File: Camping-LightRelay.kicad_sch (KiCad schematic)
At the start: 61 parts, among them CN1 U262-061N-4BVC11, CN2 907-152A1022D10200, CN3 907-152A1022D10200, J1 Conn_01x04_Pin, J2 Conn_01x04_Socket, Q1 FDV301N, Q2 BC817, Q3 IRF7404, U1 USBLC6-2SC6, U2 CD4011UBM, U3 SI1865DDL, U4 ME2108A50M, U5 TLC555DTR

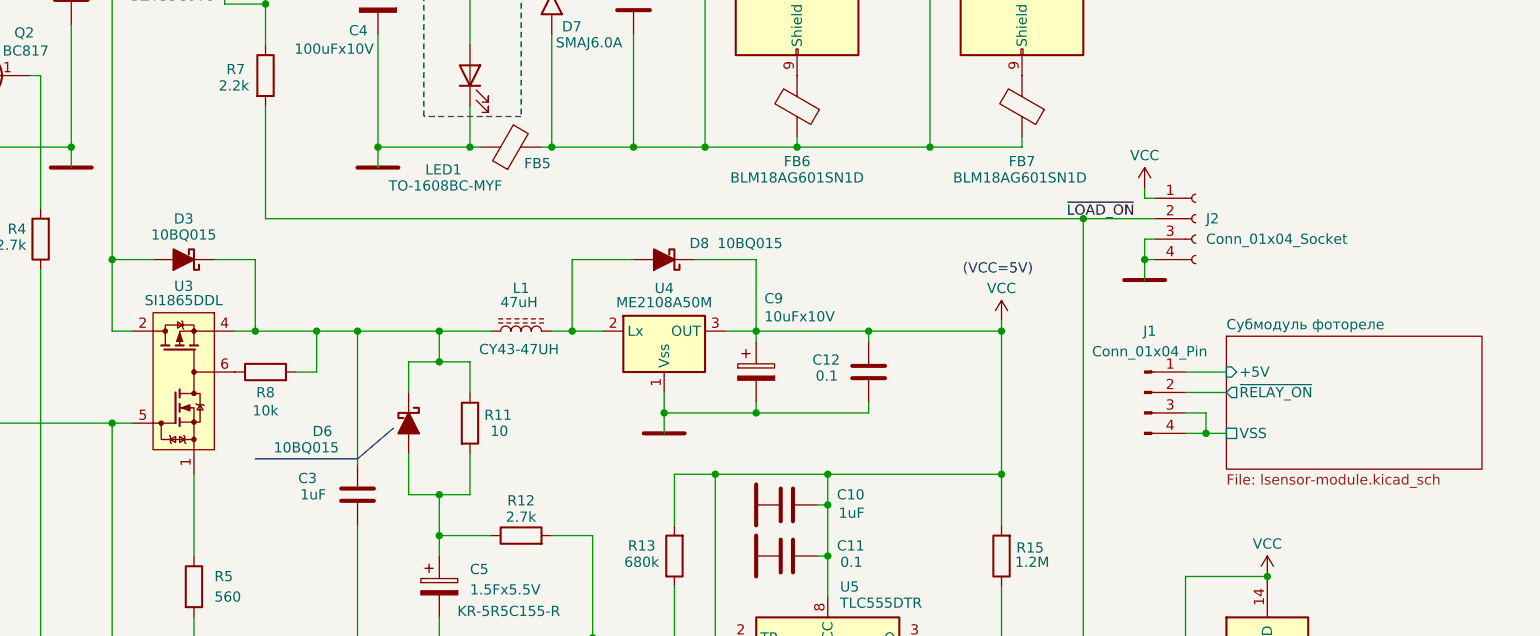
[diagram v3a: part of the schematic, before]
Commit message: Назначение посадочных мест схемы
Дорисовка недостающий э/компонентов и важных 3D-моделей
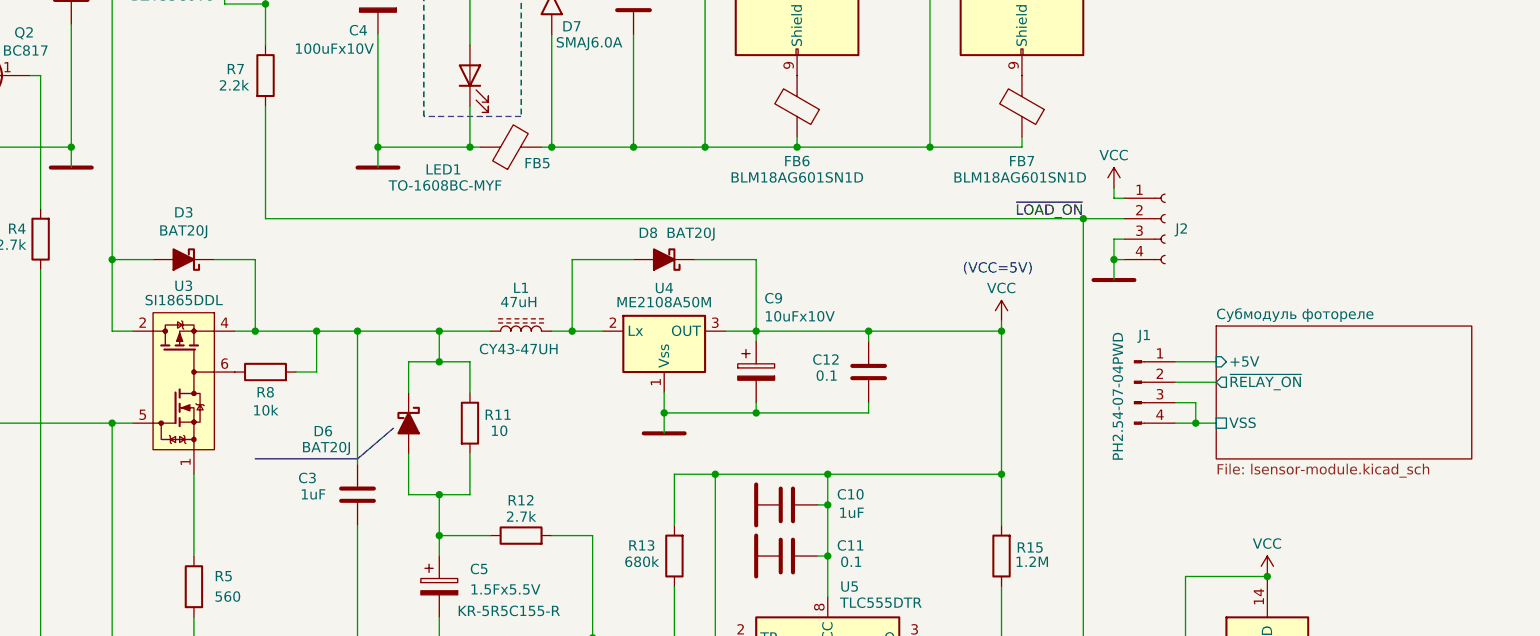
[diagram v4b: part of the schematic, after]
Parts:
- removed D3, D6, D8: 10BQ015, Diode_SMD_AKL:D_SMB, symbol PCM_Diode_Schottky_AKL:VS-10BQ015
- added D3, D6, D8: BAT20J, Diode_SMD:D_SOD-323_HandSoldering, symbol PCM_Diode_Schottky_AKL:BAT20J
- C10: footprint (none) -> Capacitor_SMD:C_0805_2012Metric
- C11, C12, C15, C6, C8: footprint (none) -> Capacitor_SMD:C_0603_1608Metric
- C5: footprint (none) -> lib:Eaton_KR-5R5C155
- J1: value Conn_01x04_Pin -> PH2.54-07-04PWD; footprint (none) -> Connector_PinHeader_2.54mm:PinHeader_1x04_P2.54mm_Horizontal
- J2: value Conn_01x04_Socket -> ~; footprint (none) -> lib:PinSolder_1x04_P2.54mm
- Q1, Q2: footprint Package_TO_SOT_SMD_AKL:SOT-23 -> PCM_Package_TO_SOT_SMD_AKL:SOT-23_BigPads
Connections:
- net VCC: now also D8.1 (K)
- net at C2.1, D4.1 (K), D5.1 (A1)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: now also D3.2 (A)
- net at C3.1, L1.1, R11.1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: now also D3.1 (K), D6.1 (K)
- net at C5.1, R11.2, R12.1: now also D6.2 (A)
- net at L1.2, U4.2 (Lx): now also D8.2 (A)
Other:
- moved on the sheet: J1, J2

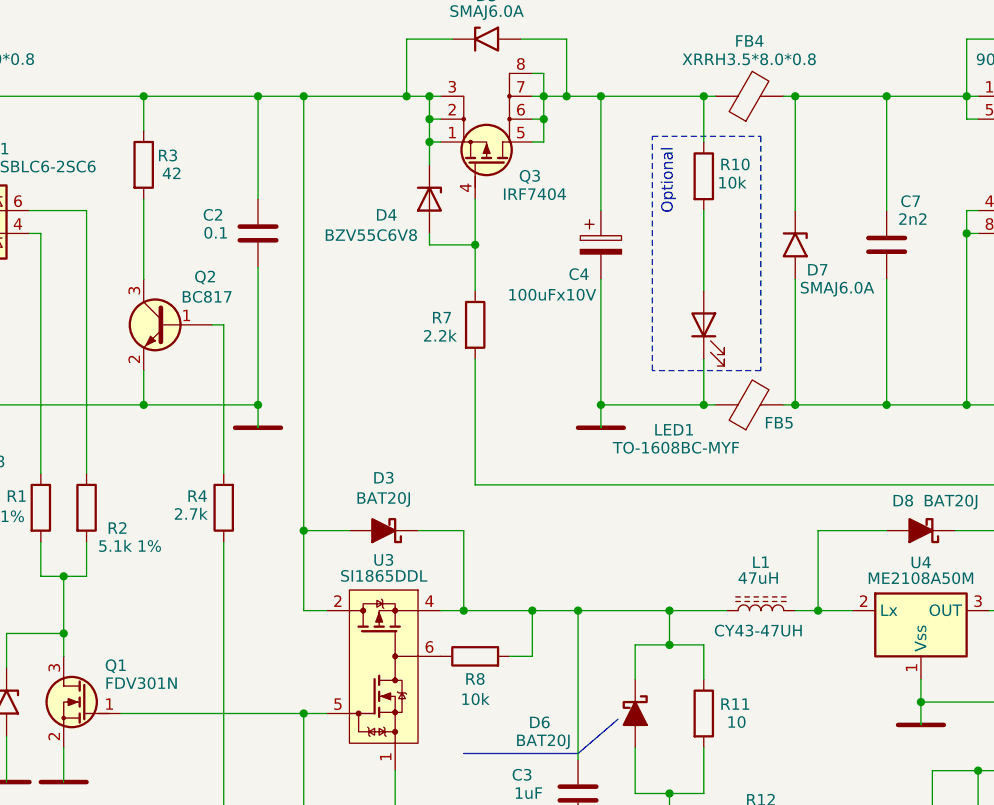
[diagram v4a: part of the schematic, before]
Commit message: Переход на 2-х стороннюю ПП
Топология ПП выбрана двусторонняя в виду миниатюрности устройства. Изменение посадочных мест под новую топологию.
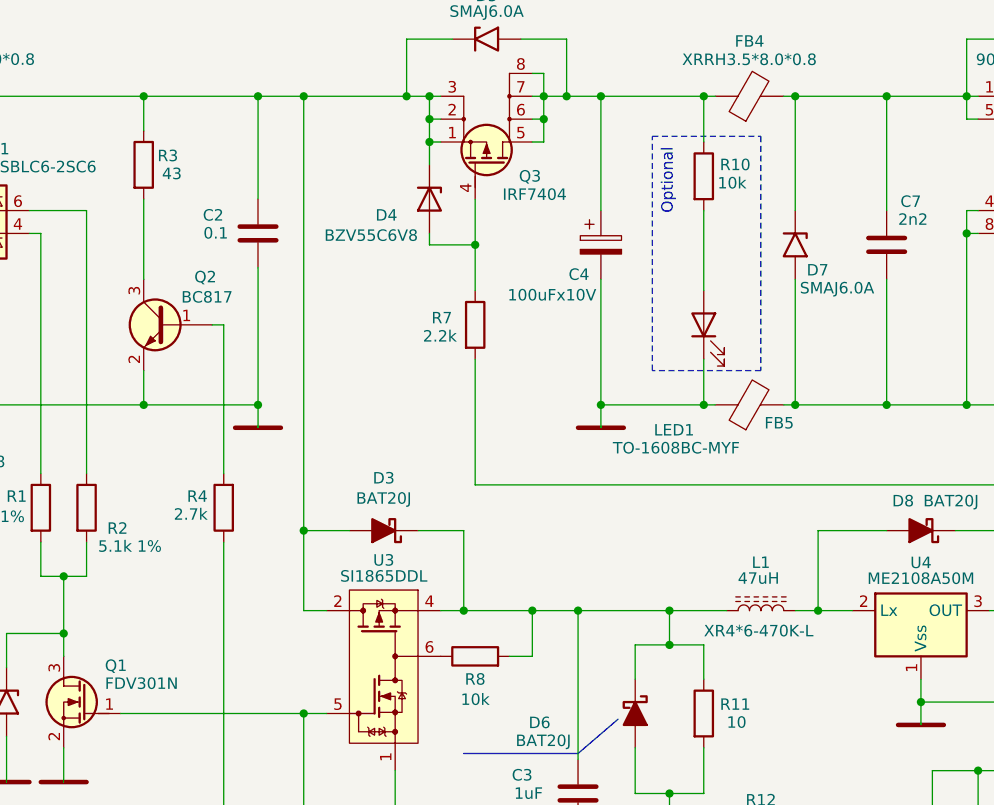
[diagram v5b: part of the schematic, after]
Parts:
- FB2, FB4: footprint PCM_Ferrite_THT_AKL:Ferrite_L8.0mm_D3.5mm_P12.70mm -> PCM_Ferrite_THT_AKL:Ferrite_L8.0mm_D3.5mm_P3.81mm_Vertical
- L1: footprint Inductor_SMD:L_Taiyo-Yuden_NR-50xx -> Inductor_THT:L_Radial_D6.0mm_P4.00mm; Part Number CY43-47UH -> XR4*6-470K-L
- Q1, Q2: footprint PCM_Package_TO_SOT_SMD_AKL:SOT-23_BigPads -> Package_TO_SOT_SMD:SOT-23
- R3: value 42 -> 43; footprint PCM_Resistor_SMD_AKL:R_0805_2012Metric_Pad1.15x1.40mm -> Resistor_THT:R_Axial_DIN0309_L9.0mm_D3.2mm_P2.54mm_Vertical
- U4: now in the parts list
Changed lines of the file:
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@@
 			)
 		)
-		(property "Footprint" "PCM_Ferrite_THT_AKL:Ferrite_L8.0mm_D3.5mm_P12.70mm"
+		(property "Footprint" "PCM_Ferrite_THT_AKL:Ferrite_L8.0mm_D3.5mm_P3.81mm_Vertical"
 			(at 69.85 30.988 90)
 			(effects
@@
 			)
 		)
-		(property "Value" "42"
+		(property "Value" "43"
 			(at 94.742 37.084 0)
 			(effects
@@
 			)
 		)
-		(property "Footprint" "PCM_Resistor_SMD_AKL:R_0805_2012Metric_Pad1.15x1.40mm"
+		(property "Footprint" "Resistor_THT:R_Axial_DIN0309_L9.0mm_D3.2mm_P2.54mm_Vertical"
 			(at 90.932 36.83 90)
 			(effects
@@
 			)
 		)
-		(property "Footprint" "PCM_Package_TO_SOT_SMD_AKL:SOT-23_BigPads"
+		(property "Footprint" "Package_TO_SOT_SMD:SOT-23"
 			(at 90.17 52.07 0)
 			(effects
@@
 			)
 		)
-		(property "Footprint" "PCM_Package_TO_SOT_SMD_AKL:SOT-23_BigPads"
+		(property "Footprint" "Package_TO_SOT_SMD:SOT-23"
 			(at 81.28 93.98 0)
 			(effects
@@
 			)
 		)
-		(property "Footprint" "PCM_Ferrite_THT_AKL:Ferrite_L8.0mm_D3.5mm_P12.70mm"
+		(property "Footprint" "PCM_Ferrite_THT_AKL:Ferrite_L8.0mm_D3.5mm_P3.81mm_Vertical"
 			(at 160.02 30.988 90)
 			(effects
@@
 			)
 		)
-		(property "Footprint" "Inductor_SMD:L_Taiyo-Yuden_NR-50xx"
+		(property "Footprint" "Inductor_THT:L_Radial_D6.0mm_P4.00mm"
 			(at 161.29 86.36 0)
 			(effects
@@
 			)
 		)
-		(property "Part Number" " CY43-47UH"
+		(property "Part Number" "XR4*6-470K-L"
 			(at 161.036 87.884 90)
 			(effects
@@
 		(unit 1)
 		(exclude_from_sim no)
-		(in_bom no)
-		(on_board no)
+		(in_bom yes)
+		(on_board yes)
 		(dnp no)
 		(property "Reference" "U4"

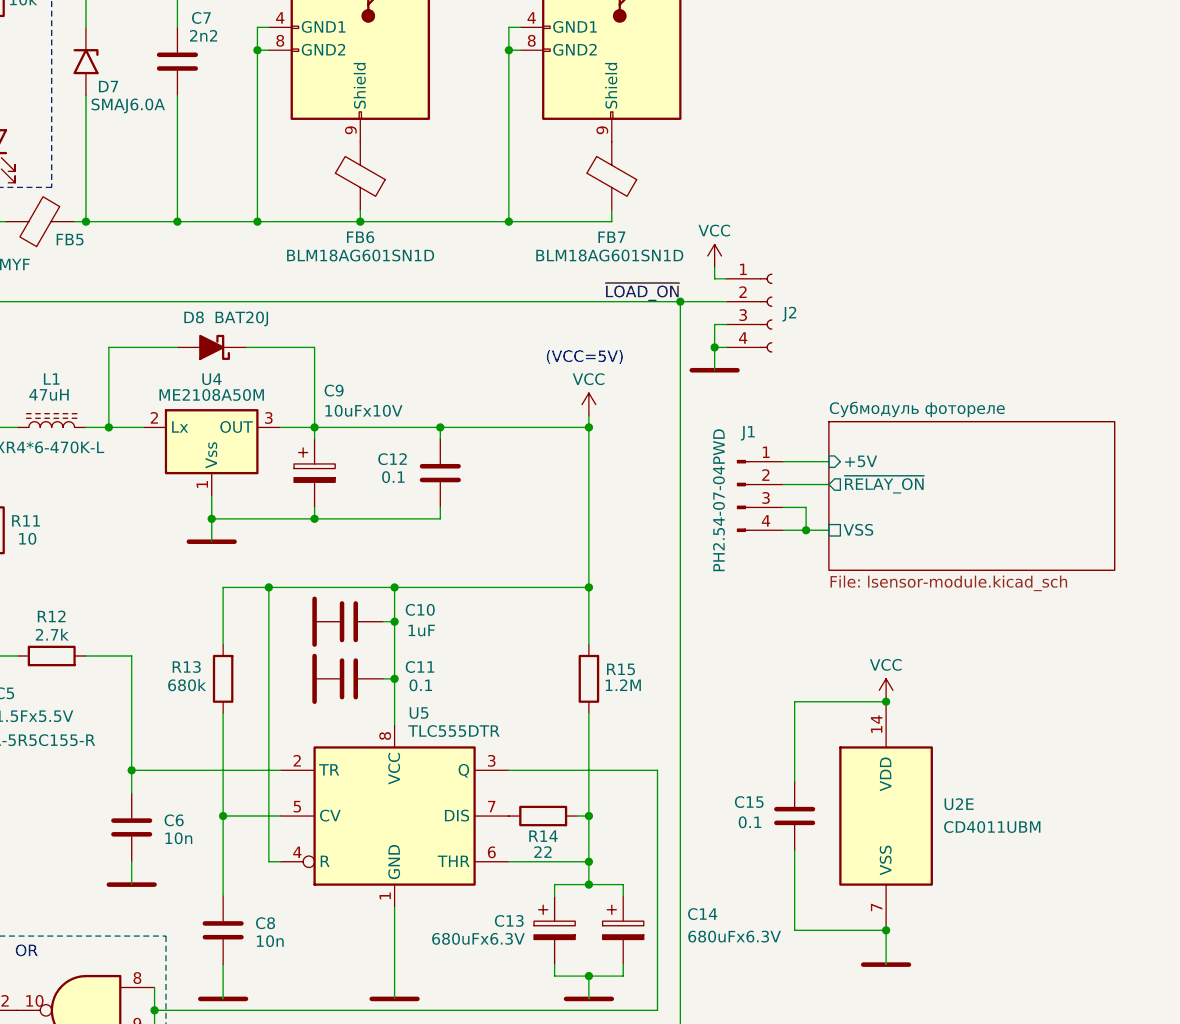
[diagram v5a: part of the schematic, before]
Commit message: Разводка ПП, трассировка, оптимизация
Отказ от идеи с субмодулем, все разводится на двухсторонней ПП.
Вынос аналогового фотореле на отдельный лист схемы.
Разводка двусторонней ПП
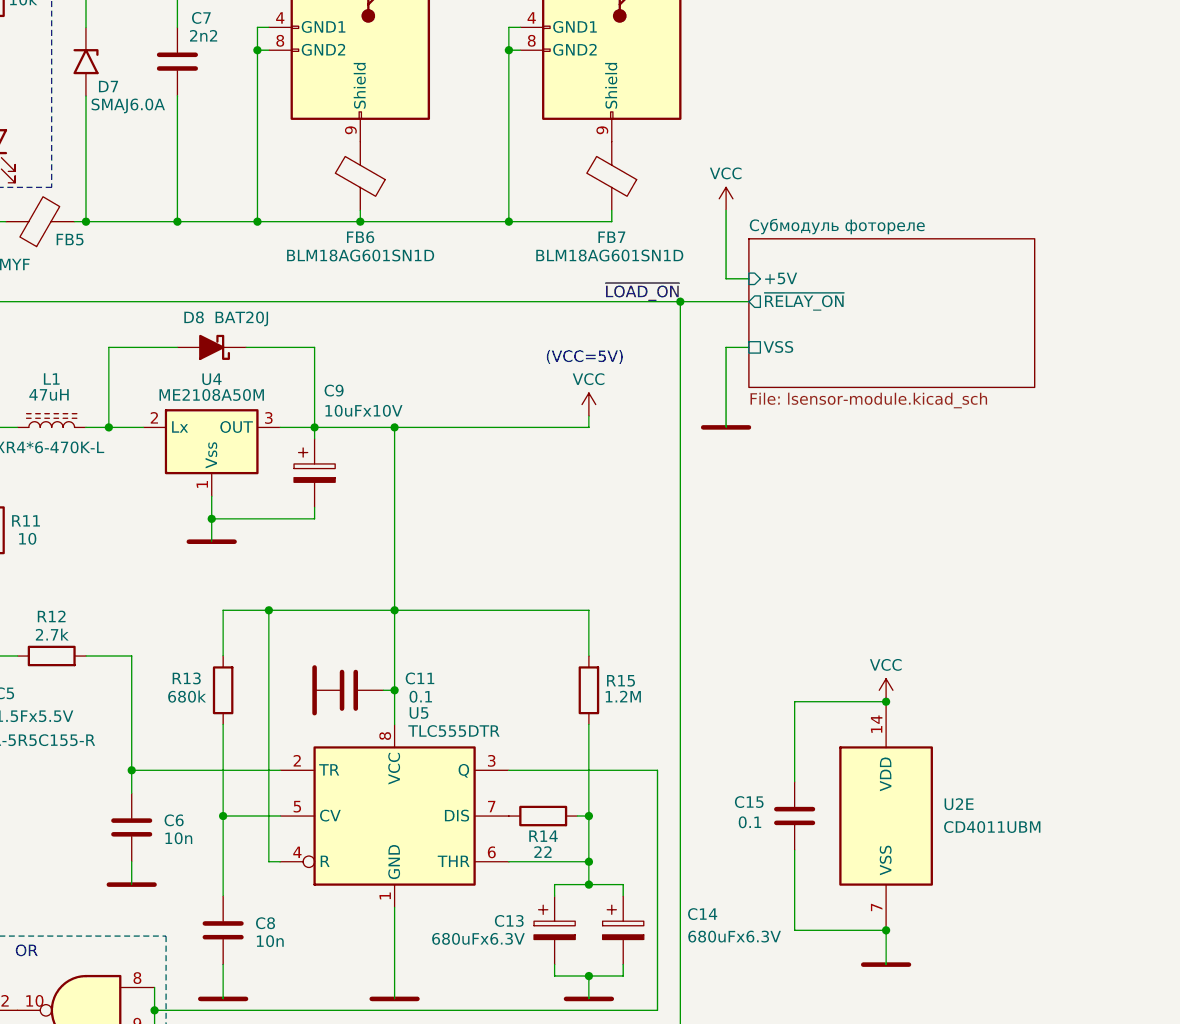
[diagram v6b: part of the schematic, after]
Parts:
- removed C10: 1uF, Capacitor_SMD:C_0805_2012Metric, symbol Device:C
- removed C12: 0.1, Capacitor_SMD:C_0603_1608Metric, symbol Device:C
- removed J1: PH2.54-07-04PWD, Connector_PinHeader_2.54mm:PinHeader_1x04_P2.54mm_Horizontal, symbol Connector:Conn_01x04_Pin
- removed J2: ~, lib:PinSolder_1x04_P2.54mm, symbol Connector:Conn_01x04_Socket
- C1, C7: footprint Capacitor_THT:C_Disc_D8.0mm_W5.0mm_P7.50mm -> PCM_Capacitor_THT_AKL:C_Disc_D7.5mm_W5.0mm_P7.50mm
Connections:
- net GND2 is gone; now on net GNDE: C11.1
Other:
- moved on the sheet: C11, R13, R15
